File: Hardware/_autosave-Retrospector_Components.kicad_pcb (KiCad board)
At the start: 4 copper layers, 60 x 110 mm, 134 parts, among them J1 SWD_Header, J2 Eurorack_10_pin_power, J3 Conn_01x08_Male, J4 Conn_01x08_Male, J5 Conn_01x08_Male, J6 Conn_01x08_Male, J7 USB_B_Micro, U1 STM32H743ZITx, U10 LM2675M-5, U11 TL072, U2 IS42S16800F-7TLI, U3 PCM5100APW, U4 SSI2164, U5 MCP6004, U6 MCP6004, U7 TL074, U8 NCV1117DT33T5G, U9 BA7807FP-E2, Y1 8MHz 20pF

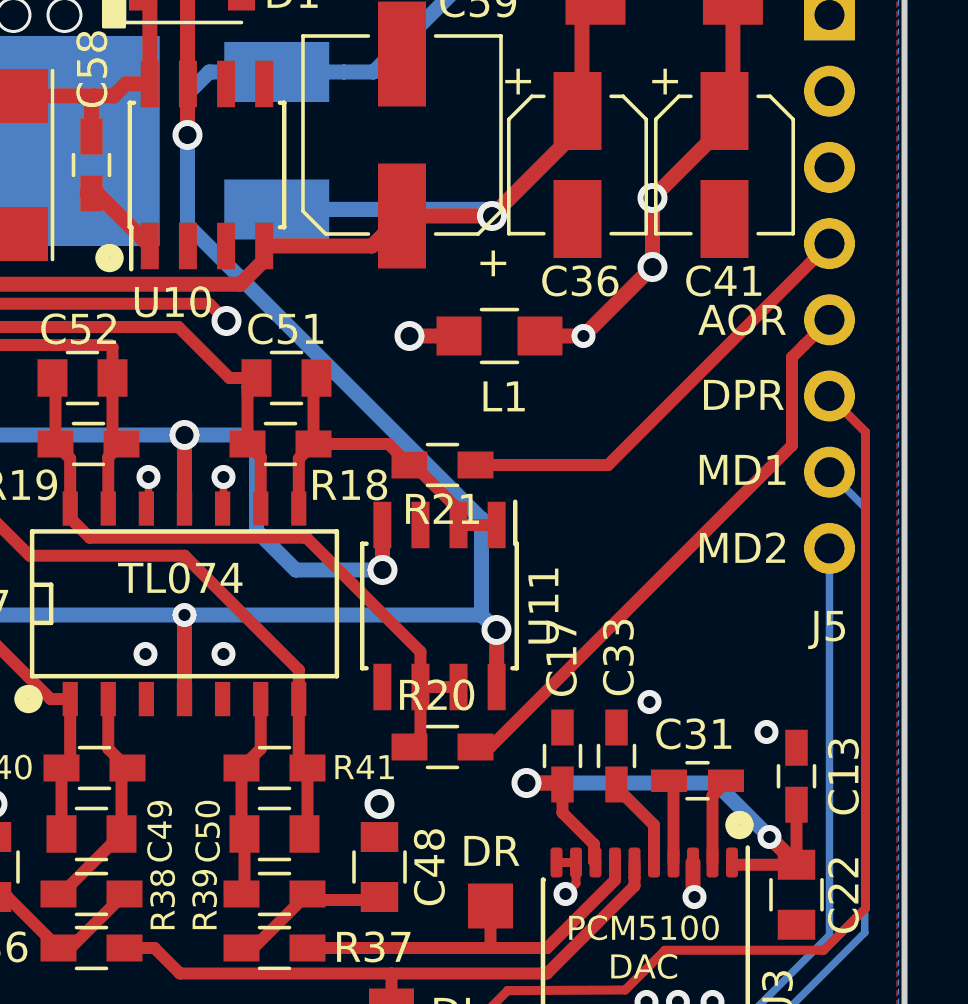
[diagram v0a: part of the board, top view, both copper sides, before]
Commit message: Include inverting op amp output stage so output is not polarity reversed
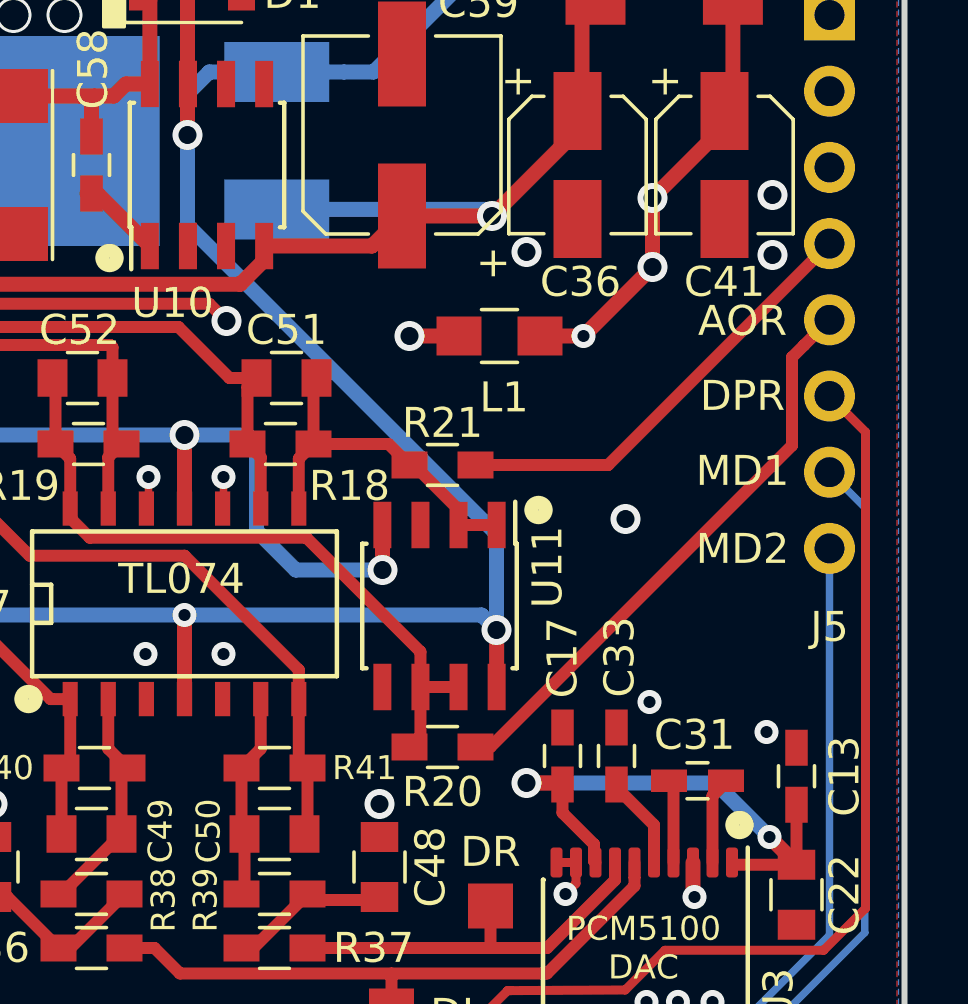
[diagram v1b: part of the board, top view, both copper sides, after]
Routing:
- net VCC: track 97.6 -> 98.3 mm
- net GND: vias 96 -> 100
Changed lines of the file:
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@@
   (general
     (thickness 1.6)
-    (drawings 49)
-    (tracks 1320)
+    (drawings 50)
+    (tracks 1324)
     (zones 0)
     (modules 134)
@@
     (tags "SOIC 1.27")
     (attr smd)
-    (fp_text reference U11 (at 0 -3.5 90) (layer F.SilkS)
+    (fp_text reference U11 (at -1.3 -3.6 90) (layer F.SilkS)
       (effects (font (size 1 1) (thickness 0.15)))
     )
@@
     (tags "resistor 0603")
     (attr smd)
-    (fp_text reference R21 (at 0 -1.5) (layer F.SilkS)
+    (fp_text reference R21 (at 0 1.4) (layer F.SilkS)
       (effects (font (size 1 1) (thickness 0.15)))
     )
@@
     (tags "resistor 0603")
     (attr smd)
-    (fp_text reference R20 (at 0.2 1.7) (layer F.SilkS)
+    (fp_text reference R20 (at 0 -1.5) (layer F.SilkS)
       (effects (font (size 1 1) (thickness 0.15)))
     )
@@
     )
   )
+  (gr_circle (center 147.8 80) (end 148 80.1) (layer F.SilkS) (width 0.5))
   (gr_text J3 (at 102.5 83.8) (layer F.SilkS)
     (effects (font (size 1 1) (thickness 0.15)))
@@
   (via (at 108.6 131.8) (size 1) (drill 0.6) (layers F.Cu B.Cu) (net 1))
   (via (at 113.8 133.6) (size 1) (drill 0.6) (layers F.Cu B.Cu) (net 1))
+  (via (at 155.6 71.5) (size 1) (drill 0.6) (layers F.Cu B.Cu) (net 1))
+  (via (at 155.6 69.5) (size 1) (drill 0.6) (layers F.Cu B.Cu) (net 1))
+  (via (at 147.4 71.4) (size 1) (drill 0.6) (layers F.Cu B.Cu) (net 1))
+  (via (at 150.7 80.3) (size 1) (drill 0.6) (layers F.Cu B.Cu) (net 1))
   (segment (start 136.1 66.934315) (end 136.1 67.5) (width 0.5) (layer B.Cu) (net 4))
   (segment (start 142.3 65.4) (end 141.325 65.4) (width 0.5) (layer B.Cu) (net 4))
@@
   (segment (start 146.405 84.005) (end 146.4 84) (width 0.5) (layer F.Cu) (net 4))
   (segment (start 136 83.5) (end 145.900001 83.500001) (width 0.5) (layer B.Cu) (net 4))
-  (segment (start 136.1 70.5) (end 136.1 67.5) (width 0.5) (layer B.Cu) (net 4))
-  (segment (start 145.900001 80.300001) (end 136.1 70.5) (width 0.5) (layer B.Cu) (net 4))
-  (segment (start 145.900001 83.500001) (end 145.900001 80.300001) (width 0.5) (layer B.Cu) (net 4))
   (segment (start 146.4 84) (end 145.900001 83.500001) (width 0.5) (layer B.Cu) (net 4))
+  (segment (start 136.1 70.5) (end 136.1 67.5) (width 0.5) (layer B.Cu) (net 4))
+  (segment (start 146.4 84) (end 146.4 80.8) (width 0.5) (layer B.Cu) (net 4))
+  (segment (start 146.4 80.8) (end 136.1 70.5) (width 0.5) (layer B.Cu) (net 4))
   (via (at 142.6 82) (size 1) (drill 0.6) (layers F.Cu B.Cu) (net 5))
   (segment (start 139.710037 82) (end 142.6 82) (width 0.5) (layer B.Cu) (net 5))
